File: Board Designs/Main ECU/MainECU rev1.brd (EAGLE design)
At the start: 120.6 x 78.9 mm, 144 parts, among them X1 CONNECTOR-37, X2 CONNECTOR-4AUTOSPORT, X3 CONNECTOR-4NANO-FIT-VERTICAL-4, X4 CONNECTOR-4NANO-FIT-VERTICAL-4

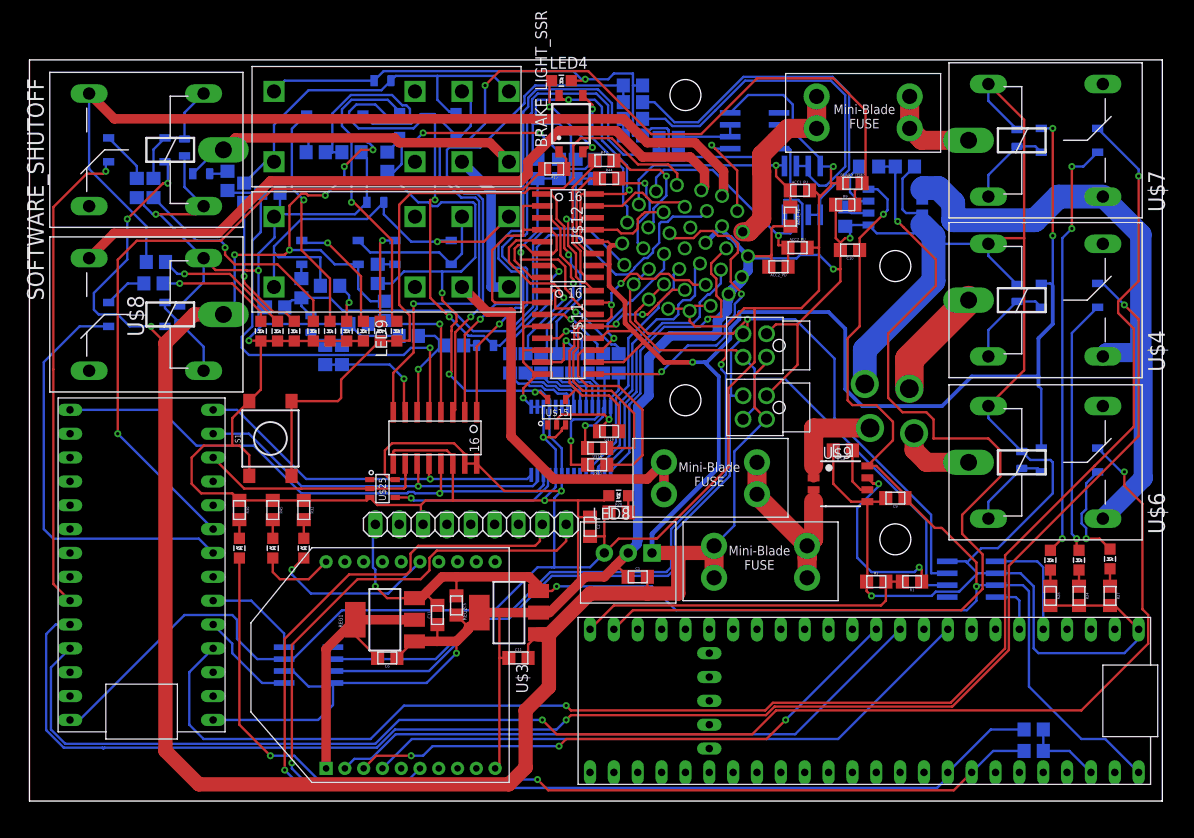
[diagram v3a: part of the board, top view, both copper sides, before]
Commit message: Fixed Wire Stubs/board outline
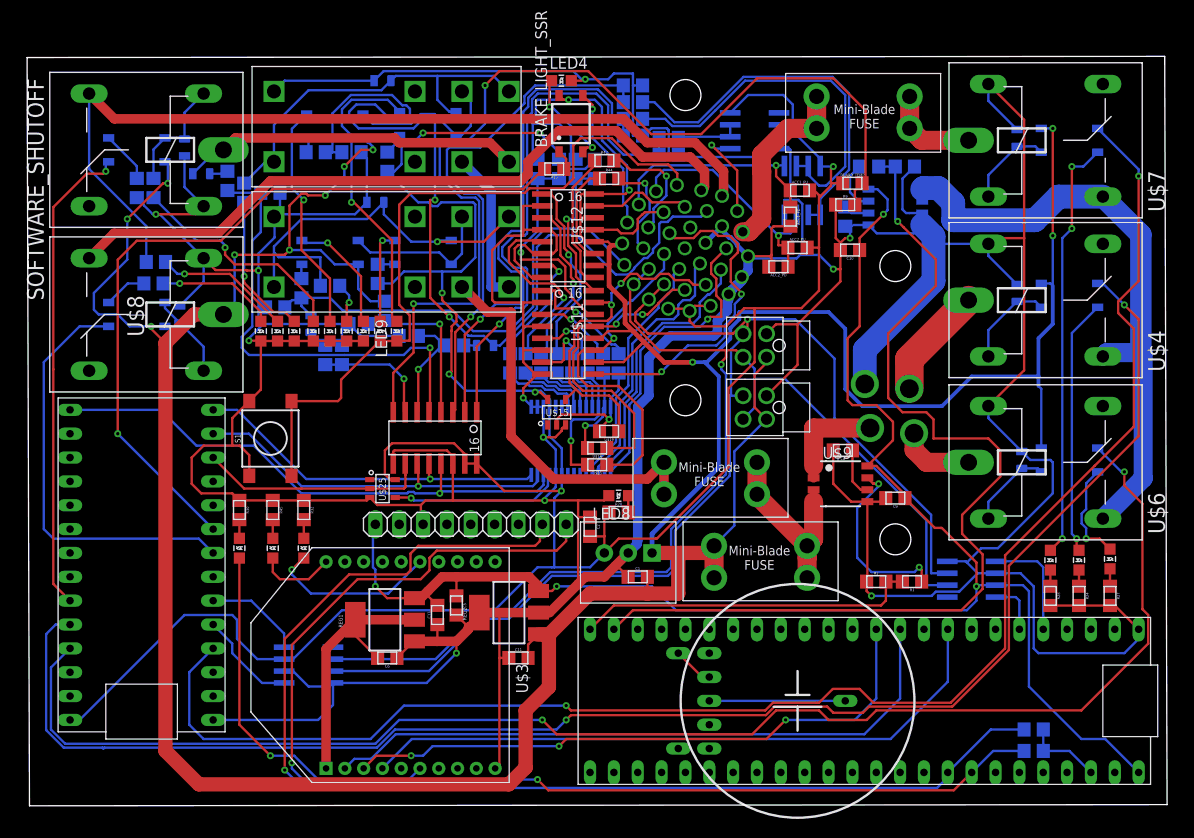
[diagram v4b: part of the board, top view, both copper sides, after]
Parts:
- added U$26: CR-2450/G1AN, HyTechDevices:CR-2450/G1AN
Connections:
- new net N$41: U$2.3.3V_2, U$26.+_0, U$26.+_1
- new net N$64: U$2.GND_2, U$26.-
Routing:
- net N$64: track 0.00 -> 14.5 mm
- net N$41: track 0.00 -> 4.35 mm
- net XBDO: track 65.3 -> 69.6 mm
- net XBDI: track 60.7 -> 65.0 mm
- net XB8: track 66.3 -> 69.6 mm
- net RELAY_CTRL2: track 165.6 -> 166.8 mm
- net GND: track 730.3 -> 729.2 mm
- net RELAY_CTRL1: track 155.9 -> 156.7 mm
- net N$32: track 16.3 -> 15.6 mm
- net RELAY_CTRL3: track 167.8 -> 168.3 mm
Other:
- board size 120.6 x 78.9 mm -> 121.4 x 79.8 mm
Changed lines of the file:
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@@
 <board>
 <plain>
-<wire x1="6.35" y1="-0.508" x2="126.98" y2="-0.508" width="0" layer="20"/>
-<wire x1="126.98" y1="-0.508" x2="126.98" y2="78.41" width="0" layer="20"/>
-<wire x1="126.98" y1="78.41" x2="6.35" y2="78.41" width="0" layer="20"/>
-<wire x1="6.35" y1="78.41" x2="6.35" y2="-0.508" width="0" layer="20"/>
+<wire x1="6.35" y1="-1.016" x2="127.488" y2="-0.889" width="0" layer="20"/>
+<wire x1="127.488" y1="-0.889" x2="127.234" y2="78.791" width="0" layer="20"/>
+<wire x1="127.234" y1="78.791" x2="6.096" y2="78.664" width="0" layer="20"/>
+<wire x1="6.096" y1="78.664" x2="6.35" y2="-1.016" width="0" layer="20"/>
 <dimension x1="126.98" y1="78.41" x2="6.35" y2="78.41" x3="66.665" y3="92.964" textsize="1.778" layer="1"/>
 <dimension x1="129.266" y1="-0.762" x2="129.266" y2="78.156" x3="145.542" y3="38.697" textsize="1.778" layer="1"/>
@@
 <element name="X3" library="HyTechDevices" package="NANO-FIT_VERTICAL-4" value="CONNECTOR-4NANO-FIT-VERTICAL-4" x="84.836" y="48.006" rot="R90"/>
 <element name="X4" library="HyTechDevices" package="NANO-FIT_VERTICAL-4" value="CONNECTOR-4NANO-FIT-VERTICAL-4" x="84.836" y="41.402" rot="R90"/>
+<element name="U$26" library="HyTechDevices" package="CR-2450/G1AN" value="CR-2450/G1AN" x="88.138" y="10.16" rot="R90"/>
 </elements>
 <signals>
@@
 <wire x1="62.383" y1="32.919" x2="62.383" y2="34.221" width="0.254" layer="16"/>
 <wire x1="61.214" y1="31.75" x2="62.383" y2="32.919" width="0.254" layer="16"/>
-<wire x1="45.085" y1="35.433" x2="45.085" y2="34.671" width="0.254" layer="1"/>
 <wire x1="51.435" y1="31.496" x2="48.514" y2="31.496" width="0.254" layer="1"/>
 <wire x1="48.514" y1="31.496" x2="48.0314" y2="31.0134" width="0.254" layer="1"/>
@@
 <wire x1="78.337303125" y1="58.940853125" x2="78.337303125" y2="58.94085625" width="0.508" layer="16"/>
 <wire x1="78.337303125" y1="58.94085625" x2="80.09743125" y2="60.700984375" width="0.508" layer="16"/>
-<wire x1="80.09743125" y1="60.700984375" x2="80.09743125" y2="60.61856875" width="0.508" layer="16"/>
 <wire x1="82.1988125" y1="54.863815625" x2="82.1988125" y2="55.29486875" width="1.016" layer="16"/>
 <wire x1="80.79789375" y1="53.462896875" x2="81.119525" y2="53.784528125" width="1.016" layer="16"/>
@@
 <wire x1="100.076" y1="62.103" x2="101.412" y2="62.103" width="0.254" layer="16"/>
 <wire x1="99.314" y1="65.777" x2="99.314" y2="62.484" width="0.254" layer="16"/>
-<wire x1="95.504" y1="60.645" x2="95.692" y2="60.833" width="0.254" layer="16"/>
-<wire x1="93.218" y1="60.697" x2="94.098" y2="60.833" width="0.254" layer="16"/>
-<wire x1="94.098" y1="60.833" x2="95.692" y2="60.833" width="0.254" layer="16"/>
+<wire x1="95.692" y1="60.833" x2="94.098" y2="60.833" width="0.254" layer="16"/>
 <wire x1="95.30115" y1="43.903615625" x2="95.30115" y2="47.54915" width="2.54" layer="16"/>
 <wire x1="102.616" y1="59.629" x2="101.412" y2="60.833" width="2.54" layer="16"/>
@@
 <wire x1="29.754" y1="36.322" x2="29.754" y2="34.125" width="0.254" layer="1"/>
 <wire x1="28.738" y1="37.338" x2="29.754" y2="36.322" width="0.254" layer="1"/>
+<wire x1="94.098" y1="60.833" x2="93.962" y2="60.697" width="0.1524" layer="16"/>
+<wire x1="93.962" y1="60.697" x2="93.218" y2="60.697" width="0.1524" layer="16"/>
 </signal>
 <signal name="+12V">
@@
 <wire x1="119.761" y1="35.179" x2="110.236" y2="25.654" width="0.254" layer="1"/>
 <wire x1="110.236" y1="25.654" x2="110.236" y2="15.748" width="0.254" layer="1"/>
-<wire x1="110.236" y1="15.748" x2="104.4448" y2="9.9568" width="0.254" layer="1"/>
-<wire x1="104.4448" y1="9.9568" x2="85.515325" y2="9.9568" width="0.254" layer="1"/>
+<wire x1="104.4448" y1="9.9568" x2="110.236" y2="15.748" width="0.254" layer="1"/>
+<wire x1="90.17" y1="9.9568" x2="90.424" y2="9.9568" width="0.254" layer="1"/>
+<wire x1="90.17" y1="9.9568" x2="85.515325" y2="9.9568" width="0.254" layer="1"/>
 <wire x1="84.702525" y1="9.144" x2="64.008" y2="9.144" width="0.254" layer="1"/>
 <wire x1="85.515325" y1="9.9568" x2="84.702525" y2="9.144" width="0.254" layer="1"/>
@@
 <wire x1="23.368" y1="13.208" x2="25.908" y2="15.748" width="0.254" layer="16"/>
 <wire x1="24.892" y1="6.096" x2="23.368" y2="7.62" width="0.254" layer="16"/>
+<wire x1="90.424" y1="9.9568" x2="91.8972" y2="11.43" width="0.254" layer="1"/>
+<wire x1="94.742" y1="11.43" x2="96.2152" y2="9.9568" width="0.254" layer="1"/>
+<wire x1="91.8972" y1="11.43" x2="94.742" y2="11.43" width="0.254" layer="1"/>
+<wire x1="96.2152" y1="9.9568" x2="104.4448" y2="9.9568" width="0.254" layer="1"/>
 </signal>
 <signal name="RELAY_CTRL1">
@@
 <wire x1="125.476" y1="19.304" x2="125.476" y2="16.256" width="0.254" layer="1"/>
 <wire x1="124.8664" y1="31.1563375" x2="124.8664" y2="19.9136" width="0.254" layer="1"/>
-<wire x1="118.364" y1="9.144" x2="85.852" y2="9.144" width="0.254" layer="1"/>
+<wire x1="96.52" y1="9.144" x2="118.364" y2="9.144" width="0.254" layer="1"/>
+<wire x1="85.852" y1="9.144" x2="90.424" y2="9.144" width="0.254" layer="1"/>
 <wire x1="85.852" y1="9.144" x2="83.312" y2="6.604" width="0.254" layer="1"/>
 <wire x1="62.484" y1="6.604" x2="60.96" y2="8.128" width="0.254" layer="1"/>
@@
 <wire x1="8.636" y1="13.716" x2="10.668" y2="15.748" width="0.254" layer="16"/>
 <wire x1="8.636" y1="7.112" x2="8.636" y2="13.716" width="0.254" layer="16"/>
+<wire x1="90.424" y1="9.144" x2="91.44" y2="8.128" width="0.254" layer="1"/>
+<wire x1="91.44" y1="8.128" x2="95.504" y2="8.128" width="0.254" layer="1"/>
+<wire x1="95.504" y1="8.128" x2="96.52" y2="9.144" width="0.254" layer="1"/>
 </signal>
 <signal name="FAN2-">
@@
 <wire x1="110.6424" y1="24.5364" x2="110.6424" y2="15.5796625" width="0.254" layer="1"/>
 <wire x1="124.46" y1="38.354" x2="110.6424" y2="24.5364" width="0.254" layer="1"/>
-<wire x1="104.6131375" y1="9.5504" x2="85.6836625" y2="9.5504" width="0.254" layer="1"/>
-<wire x1="85.6836625" y1="9.5504" x2="84.7692625" y2="8.636" width="0.254" layer="1"/>
+<wire x1="95.758" y1="9.5504" x2="104.6131375" y2="9.5504" width="0.254" layer="1"/>
+<wire x1="84.7692625" y1="8.636" x2="85.6836625" y2="9.5504" width="0.254" layer="1"/>
 <wire x1="110.6424" y1="15.5796625" x2="104.6131375" y2="9.5504" width="0.254" layer="1"/>
 <wire x1="64.008" y1="8.636" x2="63.5" y2="8.128" width="0.254" layer="1"/>
@@
 <wire x1="8.128" y1="17.272" x2="9.144" y2="18.288" width="0.254" layer="16"/>
 <wire x1="9.144" y1="18.288" x2="10.668" y2="18.288" width="0.254" layer="16"/>
+<wire x1="91.2876" y1="9.5504" x2="91.948" y2="8.89" width="0.254" layer="1"/>
+<wire x1="91.948" y1="8.89" x2="95.0976" y2="8.89" width="0.254" layer="1"/>
+<wire x1="95.0976" y1="8.89" x2="95.758" y2="9.5504" width="0.254" layer="1"/>
+<wire x1="85.6836625" y1="9.5504" x2="91.2876" y2="9.5504" width="0.254" layer="1"/>
 </signal>
 <signal name="CURRENTSENSE2">
@@
 <contactref element="LED7" pad="A"/>
 <wire x1="29.21" y1="63.237" x2="29.21" y2="55.372" width="0.254" layer="16"/>
-<wire x1="34.544" y1="50.58" x2="35.018" y2="51.054" width="0.254" layer="1"/>
 <wire x1="34.544" y1="50.58" x2="33.562" y2="51.562" width="0.254" layer="1"/>
 <wire x1="33.562" y1="51.562" x2="32.3247375" y2="51.562" width="0.254" layer="1"/>
@@
 <contactref element="U$2" pad="D9(RX2)"/>
 <wire x1="42.728" y1="3.986" x2="45.346" y2="6.604" width="0.254" layer="16"/>
-<wire x1="87.884" y1="6.604" x2="99.06" y2="17.78" width="0.254" layer="16"/>
-<wire x1="45.346" y1="6.604" x2="87.884" y2="6.604" width="0.254" layer="16"/>
+<wire x1="95.25" y1="6.604" x2="99.06" y2="10.414" width="0.254" layer="16"/>
+<wire x1="45.346" y1="6.604" x2="95.25" y2="6.604" width="0.254" layer="16"/>
 <wire x1="40.95" y1="3.986" x2="42.728" y2="3.986" width="0.254" layer="16"/>
 <wire x1="39.934" y1="2.97" x2="40.95" y2="3.986" width="0.254" layer="16"/>
+<wire x1="99.06" y1="10.414" x2="99.06" y2="17.78" width="0.254" layer="16"/>
 </signal>
 <signal name="XBDI">
@@
 <wire x1="84.836" y1="6.096" x2="63.5" y2="6.096" width="0.254" layer="1"/>
 <via x="86.868" y="8.128" extent="1-16" drill="0.35"/>
-<wire x1="96.52" y1="17.78" x2="86.868" y2="8.128" width="0.254" layer="16"/>
+<wire x1="96.52" y1="10.414" x2="94.234" y2="8.128" width="0.254" layer="16"/>
 <via x="46.99" y="4.318" extent="1-16" drill="0.35"/>
 <via x="62.738" y="5.334" extent="1-16" drill="0.35"/>
@@
 <wire x1="48.26" y1="4.318" x2="46.99" y2="4.318" width="0.254" layer="16"/>
 <wire x1="41.934" y1="2.97" x2="43.282" y2="4.318" width="0.254" layer="1"/>
+<wire x1="96.52" y1="17.78" x2="96.52" y2="10.414" width="0.254" layer="16"/>
+<wire x1="94.234" y1="8.128" x2="86.868" y2="8.128" width="0.254" layer="16"/>
 </signal>
 <signal name="XB8">
@@
 <contactref element="U$2" pad="D7(RX3)"/>
 <wire x1="43.934" y1="2.97" x2="47.06" y2="6.096" width="0.254" layer="16"/>
-<wire x1="92.456" y1="6.096" x2="104.14" y2="17.78" width="0.254" layer="16"/>
-<wire x1="47.06" y1="6.096" x2="92.456" y2="6.096" width="0.254" layer="16"/>
+<wire x1="98.044" y1="6.096" x2="104.14" y2="12.192" width="0.254" layer="16"/>
+<wire x1="47.06" y1="6.096" x2="98.044" y2="6.096" width="0.254" layer="16"/>
+<wire x1="104.14" y1="12.192" x2="104.14" y2="17.78" width="0.254" layer="16"/>
 </signal>
 <signal name="N$45">
@@
 <wire x1="84.3054" y1="66.542375" x2="84.3054" y2="68.3034" width="2.032" layer="1"/>
 </signal>
+<signal name="N$41">
+<contactref element="U$2" pad="3.3V_2"/>
+<contactref element="U$26" pad="+_0"/>
+<contactref element="U$26" pad="+_1"/>
+<wire x1="75.438" y1="15.24" x2="77.978" y2="12.7" width="0.254" layer="1"/>
+<wire x1="77.978" y1="12.7" x2="78.74" y2="12.7" width="0.254" layer="1"/>
+<wire x1="75.438" y1="5.08" x2="77.978" y2="12.7" width="0" layer="19" extent="1-1"/>
+</signal>
+<signal name="N$64">
+<contactref element="U$26" pad="-"/>
+<contactref element="U$2" pad="GND_2"/>
+<wire x1="78.74" y1="10.16" x2="93.218" y2="10.16" width="0.254" layer="16"/>
+</signal>
 </signals>

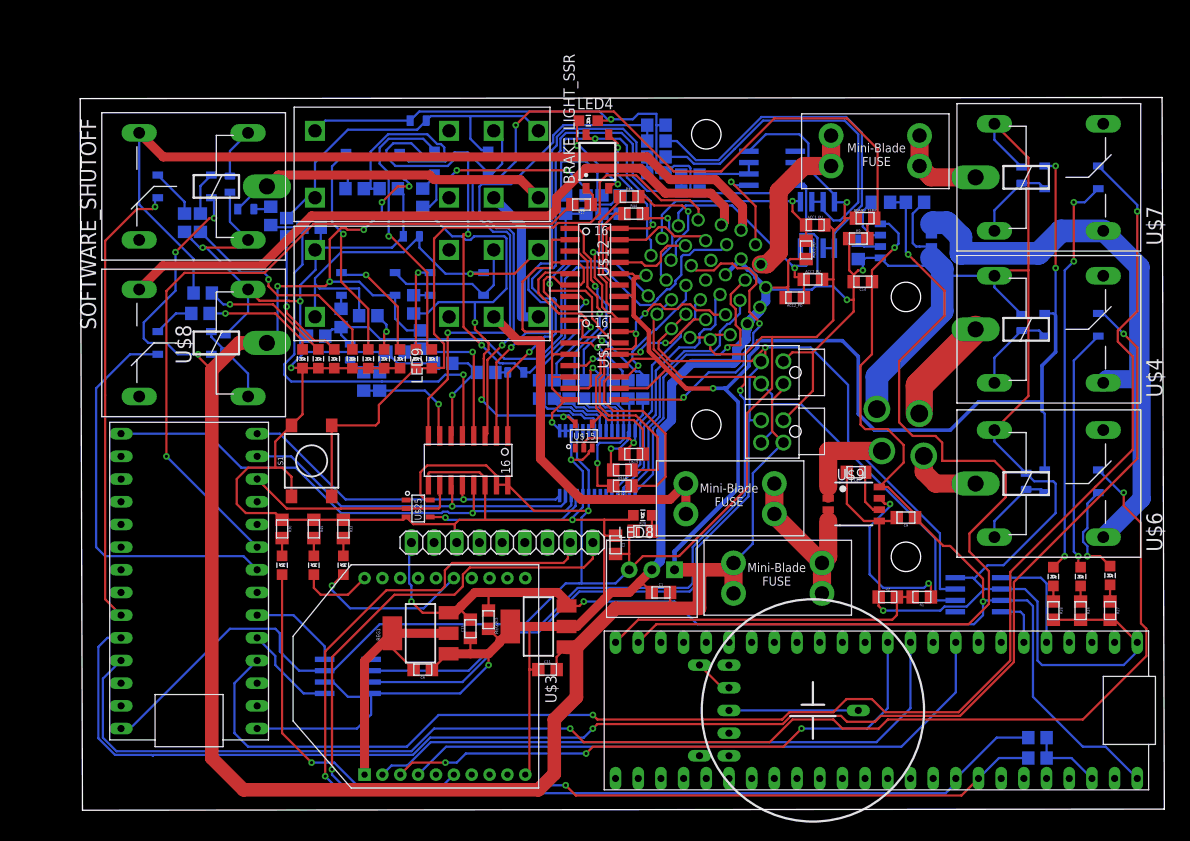
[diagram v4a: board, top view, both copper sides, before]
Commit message: Update BMS adapter rev3 and MainECU rev{1,2} for manufacturing, update Advanced Circuits DRC to reflect new min drill size
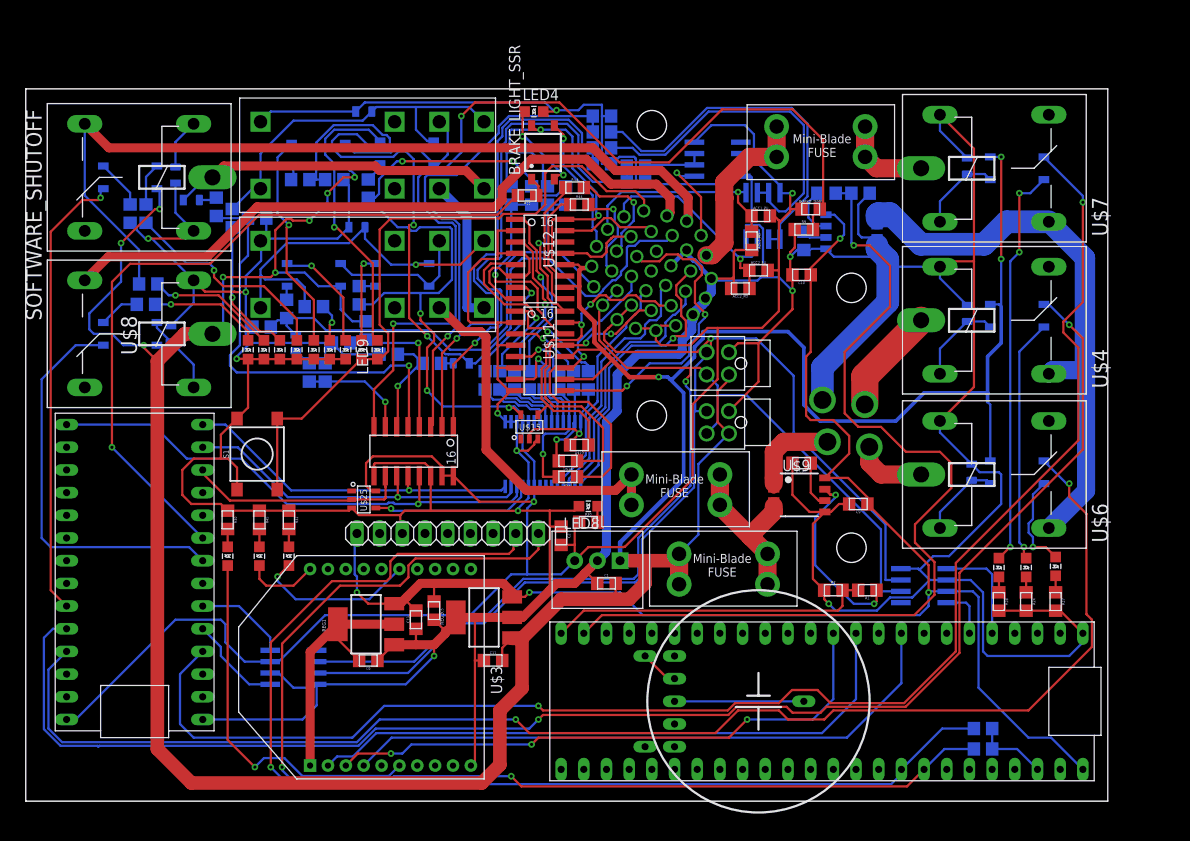
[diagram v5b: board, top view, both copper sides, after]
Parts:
- moved C10 6.90 mm to (86.9, 58.9)
- moved LED17 6.31 mm to (30.4, 50.5)
- moved ADXL345_BREAKOUT 6.18 mm to (46.0, 30.0)
- moved BMS_LATCH_SSR 6.18 mm to (42.7, 72.6)
- moved BMS_SSR 6.18 mm to (32.8, 72.4)
- moved BR_FILTR 6.18 mm to (68.3, 71.1)
- moved C1 6.18 mm to (65.0, 24.4)
- moved C12 6.18 mm to (68.3, 69.3)
- moved D8 6.18 mm to (105.4, 71.1)
- moved LED12 6.18 mm to (115.3, 26.3)
- moved R13 6.18 mm to (38.4, 68.6)
- moved R19 6.18 mm to (34.5, 69.6)
- moved R24 6.18 mm to (112.0, 22.4)
- moved R27 6.18 mm to (115.3, 22.4)
- moved R28 6.18 mm to (109.0, 22.4)
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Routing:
- net N$47: track 39.9 -> 41.8 mm
- net LATCH_EXT_BUTTON: track 76.7 -> 74.9 mm
- net BMS_OK: track 100.5 -> 99.4 mm
- net 12VUNFUSED: track 20.8 -> 19.6 mm
- net N$3: track 19.4 -> 20.3 mm
- net GND: track 729.2 -> 730.1 mm
- net +12V: track 431.7 -> 430.9 mm
- net CURRENTSENSE2: track 66.3 -> 67.1 mm
- net 12VIN: track 11.3 -> 10.7 mm
- net TELEMETRY5V: track 167.8 -> 168.3 mm
- net IMD_COIL_PWR: track 44.6 -> 44.1 mm
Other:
- board size 121.4 x 79.8 mm -> 121.2 x 79.8 mm
- board text added: "BMS Coil"
- board text added: "IMD OK"
- board text removed: "BMSCoil"
- board text removed: "IMDOK"
